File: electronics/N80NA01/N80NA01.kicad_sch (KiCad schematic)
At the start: 154 parts, among them J2 Conn_02x28_Top_Bottom, Q1 Q_PNP, Q10 Q_PNP, Q11 Q_NPN, Q12 Q_PNP, Q13 Q_NPN, Q14 Q_PNP, Q15 Q_PNP, Q16 Q_NPN, Q17 Q_PNP, Q18 Q_NPN, Q19 Q_PNP, Q2 Q_NPN, Q20 Q_NPN, Q21 Q_PNP, Q22 Q_NPN, Q23 Q_NPN, Q24 Q_PNP, Q25 Q_PNP, Q26 Q_NPN, Q27 Q_PNP, Q28 Q_NPN, Q29 Q_PNP, Q3 Q_PNP, Q30 Q_NPN, Q31 Q_NPN, Q32 Q_PNP, Q33 Q_NPN, Q34 Q_NPN, Q4 Q_NPN, Q5 Q_PNP, Q6 Q_NPN, Q7 Q_NPN, Q8 Q_PNP, Q9 Q_NPN, U1 LM741, U2 LM741, U3 LM741, U4 LM741, U5 LM741, U6 LM741

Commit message: Updated N80NA01 board
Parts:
- renumbered J2 to J1
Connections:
- net IN(X) renamed IN(IMAGE_SHIFT_X)
- net IN(Y) renamed IN(IMAGE_SHIFT_Y)
- net NF(X) renamed NF(IMAGE_SHIFT_X)
- net NF(Y) renamed NF(IMAGE_SHIFT_Y)
- net PIN10 renamed IMAGE_SHIFT_REF-
- net PINM renamed IMAGE_SHIFT_REF+
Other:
- note added: "Image Shift Amplifiers"
- moved on the sheet: C1, C10, C11, C12, C13, C14, C15, C16, C17, C18, C2, C21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

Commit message: Added more detail to Probe & CRT drive schematic
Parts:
- removed C10, C13, C14, C15, C16, C17, C18, C23, C24, C27, C28, C3, C4, C9: 4.7n, symbol Device:C
- removed C12, C8: 1u, symbol Device:C
- removed C29, C30: 10p, symbol Device:C
- removed Q1, Q10, Q12, Q14, Q15, Q17, Q19, Q21, Q24, Q25, Q27, Q29, Q3, Q32, Q5, Q8: Q_PNP, symbol Device:Q_PNP
- removed Q11, Q13, Q16, Q18, Q2, Q20, Q22, Q23, Q26, Q28, Q30, Q31, Q33, Q34, Q4, Q6, Q7, Q9: Q_NPN, symbol Device:Q_NPN
- removed R1, R12: 2.5k, symbol Device:R
- removed R10, R33, R67: 150k, symbol Device:R
- removed R11, R34, R36, R9: 30k, symbol Device:R
- removed R13, R30, R37, R4, R44, R54: 1k, symbol Device:R
- removed R14, R16, R32, R35, R38, R40, R42 (x2), R46, R47, R53, R70, R8: 10k, symbol Device:R
- removed R15, R17, R39, R41, R43, R45, R48, R49: 3k, symbol Device:R
- removed R19, R24, R62, R64: 360, symbol Device:R
- removed R2, R29: 2k, symbol Device:R
- removed R20, R23: 1.5k, symbol Device:R
- removed R22, R25: 51, symbol Device:R
- removed R26, R7: 15k, symbol Device:R
- removed R27, R31, R5, R6: 43k, symbol Device:R
- removed R28, R3: 7.5k, symbol Device:R
- removed R49, R52, R68: 100k, symbol Device:R
- removed R65, R66: 620, symbol Device:R
- removed R69: 20k, symbol Device:R
- removed R71: 39k, symbol Device:R
- removed RV1, RV2, RV3, RV4, RV8: 10k, symbol Device:R_Potentiometer_Trim
- removed RV10, RV9: 5k, symbol Device:R_Potentiometer
- removed RV5: 20k, symbol Device:R_Potentiometer_Trim
- removed RV6, RV7: 5k, symbol Device:R_Potentiometer_Trim
- removed TP1: PROBE H, symbol Connector:TestPoint
- removed TP2: PROBE V, symbol Connector:TestPoint
- removed TP3: CRT H, symbol Connector:TestPoint
- removed TP4: CRT V, symbol Connector:TestPoint
- removed U1, U2, U3, U4, U5, U6: LM741, symbol Amplifier_Operational:LM741
- renumbered J1 to PCB_EDGE
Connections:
- net PROBE_Vref+: now reaches C11.1, D2.1 (K), R21.2, R61.1
- net PROBE_Vref-: now reaches C7.2, D1.2 (A), R18.1, R63.1
- net CRT_Vref+: now reaches C22.1, D4.1 (K), R51.2
- net CRT_Vref-: now reaches C21.2, D3.2 (A), R50.1
- net PIN6 renamed MAG_SWITCH(H)
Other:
- added sheet Horizontal CRT Drive (CRT_H.kicad_sch)
- added sheet Horizontal Probe Drive (PROBE_H.kicad_sch)
- added sheet Image Shift X Drive (IMAGE_SHIFT_X.kicad_sch)
- added sheet Image Shift Y Drive (IMAGE_SHIFT_Y.kicad_sch)
- added sheet Vertical CRT Drive (CRT_V.kicad_sch)
- added sheet Vertical Probe Drive (PROBE_V.kicad_sch)
- note removed: "Image Shift Amplifiers"
- moved on the sheet: C1, C11, C2, C21, C22, C25, C26, C7, D1, D2, D3, D4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

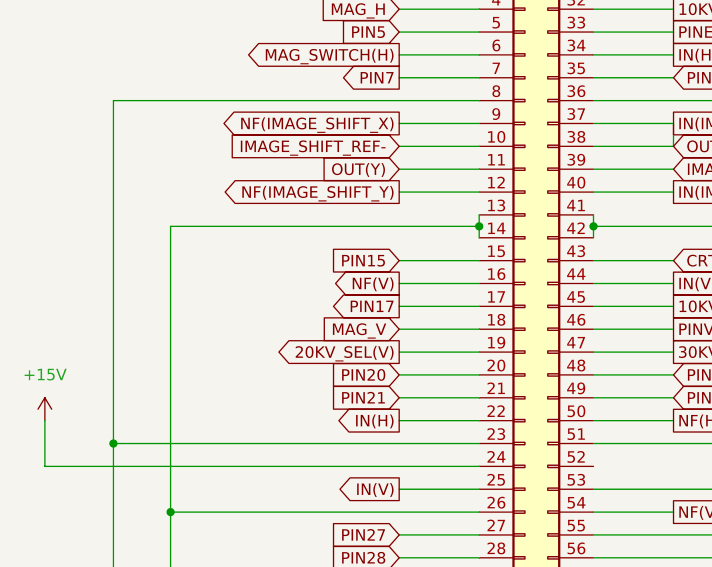
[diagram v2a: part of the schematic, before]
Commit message: Updated the probe driver schematics
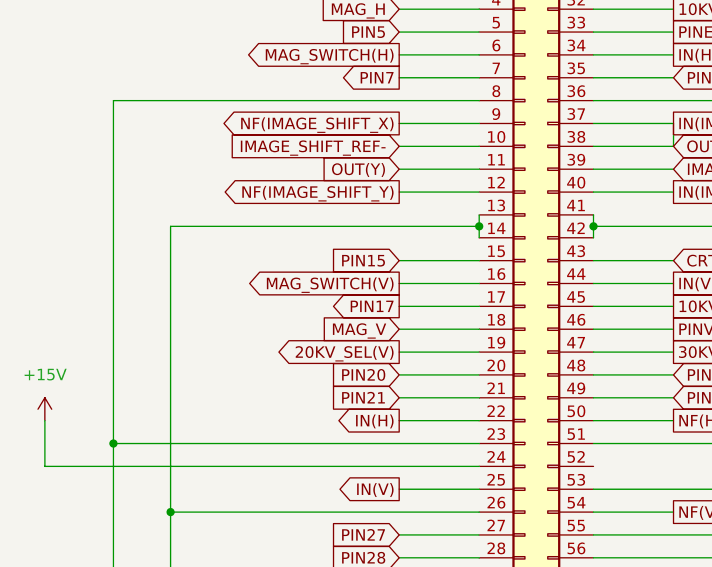
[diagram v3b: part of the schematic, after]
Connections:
- net NF(V): no longer PCB_EDGE.16 (Pin_16)
- new net MAG_SWITCH(V): PCB_EDGE.16 (Pin_16)
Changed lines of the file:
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@@
 		)
 	)
-	(global_label "NF(V)"
+	(global_label "MAG_SWITCH(V)"
 		(shape output)
 		(at 71.12 80.01 180)
@@
 		)
 		(property "Intersheetrefs" "${INTERSHEET_REFS}"
-			(at 62.9337 80.01 0)
+			(at 53.7414 80.01 0)
 			(effects
 				(font
